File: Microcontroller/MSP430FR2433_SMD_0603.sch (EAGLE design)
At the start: 8 parts, among them IC2 MSP430FR2433IRGET, Q8 32.768

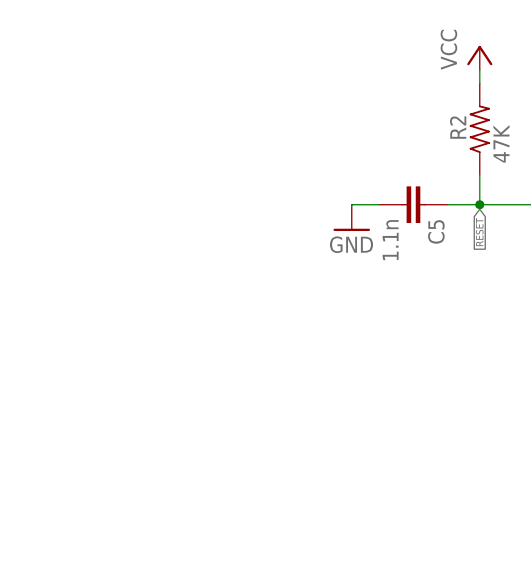
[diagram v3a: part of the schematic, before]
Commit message: masp430fr2433 modified
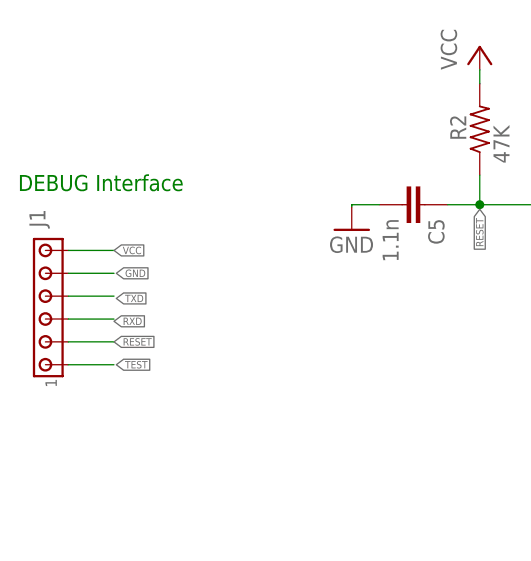
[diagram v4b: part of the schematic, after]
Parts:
- added J1: (no value), con-amp:MTA06-100
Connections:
- net GND: now also J1.5
- net RESET: now also J1.2
- net RXD: now also J1.3
- net TEST: now also J1.1
- net TXD: now also J1.4
- net VCC: now also J1.6
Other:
- note added: "DEBUG Interface"
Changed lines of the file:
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@@
 <part name="GND6" library="supply1" deviceset="GND" device=""/>
 <part name="GND7" library="supply1" deviceset="GND" device=""/>
+<part name="J1" library="con-amp" deviceset="MTA06-100" device=""/>
 </parts>
 <sheets>
 <sheet>
 <plain>
+<text x="78.232" y="136.144" size="1.778" layer="91">DEBUG Interface</text>
 </plain>
 <instances>
@@
 <instance part="GND6" gate="1" x="282.956" y="115.316"/>
 <instance part="GND7" gate="1" x="242.824" y="139.7" rot="R180"/>
+<instance part="J1" gate="G$1" x="81.28" y="121.92" rot="R90"/>
 </instances>
 <busses>
@@
 <pinref part="IC2" gate="G$1" pin="!RST!/NMI/SBWTDIO"/>
 <label x="129.54" y="134.112" size="0.8128" layer="95" rot="R270" xref="yes"/>
+</segment>
+<segment>
+<pinref part="J1" gate="G$1" pin="2"/>
+<wire x1="83.82" y1="119.38" x2="88.9" y2="119.38" width="0.1524" layer="91"/>
+<label x="88.9" y="119.38" size="0.8128" layer="95" xref="yes"/>
 </segment>
 </net>
@@
 <pinref part="GND7" gate="1" pin="GND"/>
 </segment>
+<segment>
+<pinref part="J1" gate="G$1" pin="5"/>
+<wire x1="83.82" y1="127" x2="88.9" y2="127" width="0.1524" layer="91"/>
+<label x="89.154" y="127" size="0.8128" layer="95" xref="yes"/>
+</segment>
 </net>
 <net name="VCC" class="0">
@@
 <pinref part="R2" gate="G$1" pin="2"/>
 <wire x1="129.54" y1="149.606" x2="129.54" y2="148.082" width="0.1524" layer="91"/>
+</segment>
+<segment>
+<pinref part="J1" gate="G$1" pin="6"/>
+<wire x1="83.82" y1="129.54" x2="88.9" y2="129.54" width="0.1524" layer="91"/>
+<label x="88.9" y="129.54" size="0.8128" layer="95" xref="yes"/>
 </segment>
 </net>
@@
 <label x="144.78" y="132.08" size="0.8128" layer="95" rot="R180" xref="yes"/>
 </segment>
+<segment>
+<pinref part="J1" gate="G$1" pin="1"/>
+<wire x1="83.82" y1="116.84" x2="88.9" y2="116.84" width="0.1524" layer="91"/>
+<label x="89.154" y="116.84" size="0.8128" layer="95" xref="yes"/>
+</segment>
 </net>
 <net name="TXD" class="0">
@@
 <wire x1="149.86" y1="129.54" x2="144.78" y2="129.54" width="0.1524" layer="91"/>
 <label x="144.78" y="129.54" size="0.8128" layer="95" rot="R180" xref="yes"/>
+</segment>
+<segment>
+<pinref part="J1" gate="G$1" pin="4"/>
+<wire x1="83.82" y1="124.46" x2="88.9" y2="124.46" width="0.1524" layer="91"/>
+<label x="89.154" y="124.206" size="0.8128" layer="95" xref="yes"/>
 </segment>
 </net>
@@
 <label x="144.78" y="127" size="0.8128" layer="95" rot="R180" xref="yes"/>
 </segment>
+<segment>
+<pinref part="J1" gate="G$1" pin="3"/>
+<wire x1="83.82" y1="121.92" x2="88.9" y2="121.92" width="0.1524" layer="91"/>
+<label x="88.9" y="121.666" size="0.8128" layer="95" xref="yes"/>
+</segment>
 </net>

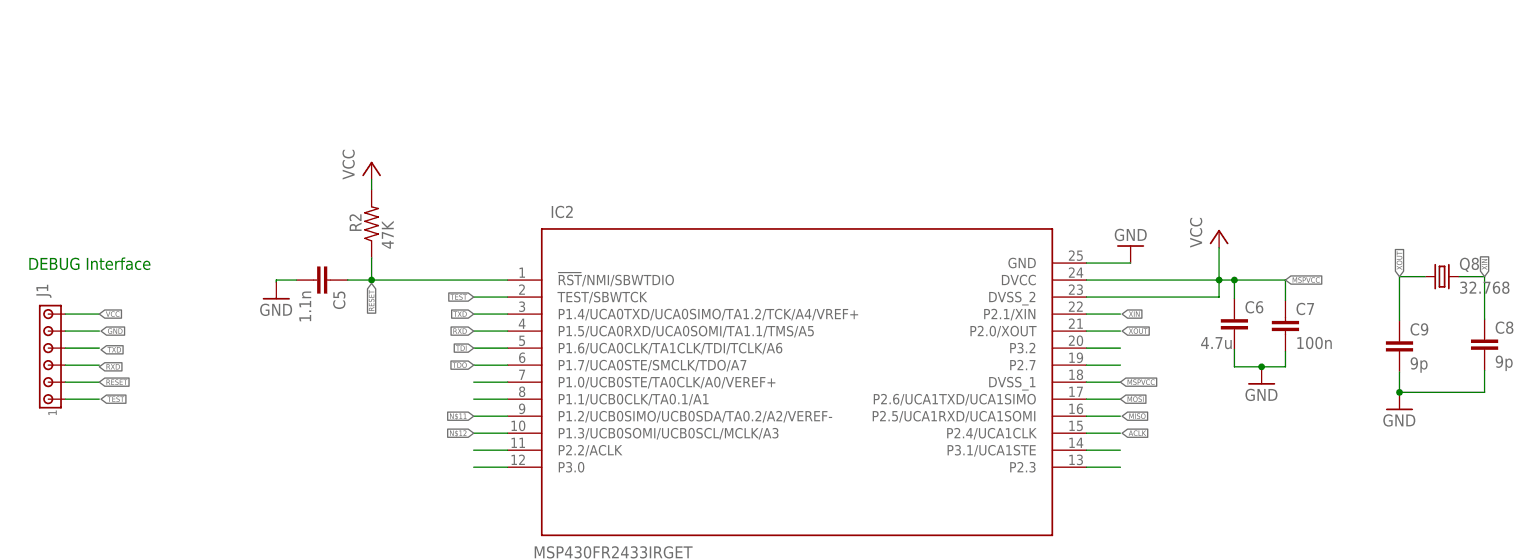
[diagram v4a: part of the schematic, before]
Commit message: masp430fr2433 modified
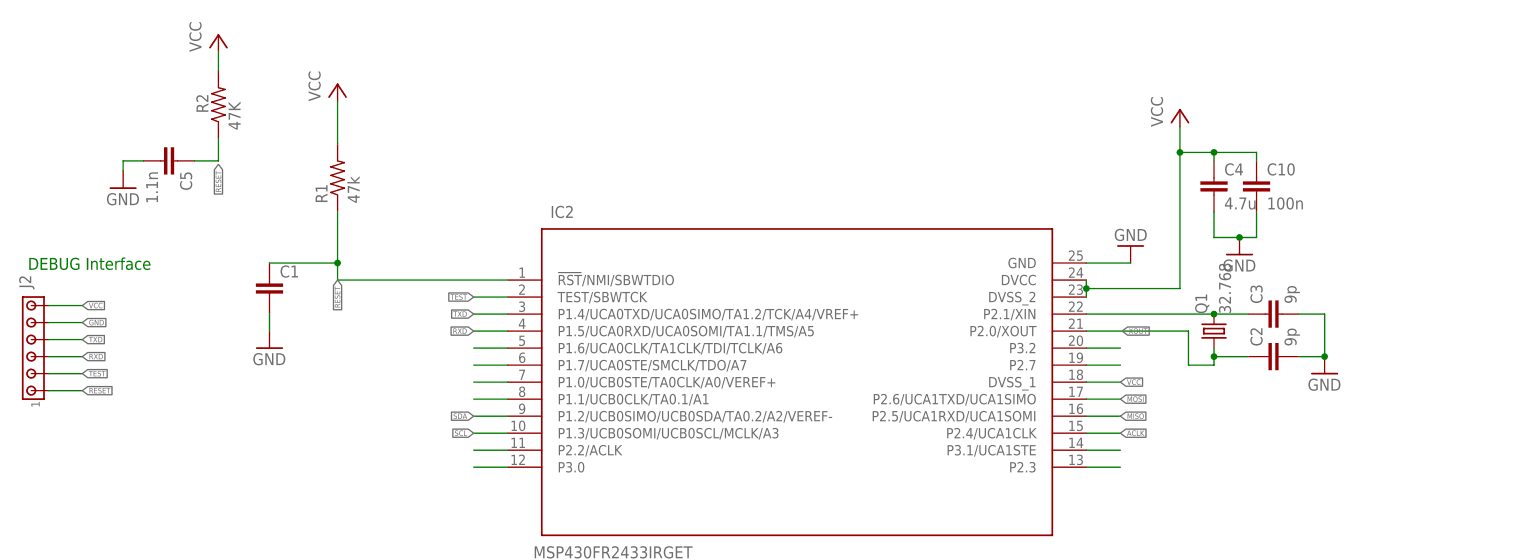
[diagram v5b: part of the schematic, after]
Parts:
- removed C6: 4.7u, rcl:C-EUC0402
- removed C7: 100n, rcl:C-EUC0402
- removed C8, C9: 9p, rcl:C-EUC0402
- removed J1: (no value), con-amp:MTA06-100
- removed Q8: 32.768, crystal:CRYTALTC26H
- added C1: (no value), rcl:C-EUC0402
- added C10: 100n, rcl:C-EUC0402
- added C2, C3: 9p, rcl:C-EUC0402
- added C4: 4.7u, rcl:C-EUC0402
- added J2: (no value), con-amp:MTA06-100
- added Q1: 32.768, crystal:CRYTALTC26H
- added R1: 47k, rcl:R-US_R0402
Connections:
- net N$11 renamed SDA
- net N$12 renamed SCL
- net TDI renamed N$7
- net TDO renamed N$8
- removed net MSPVCC: C6.1, C7.1, IC2.DVCC, IC2.DVSS_1, IC2.DVSS_2
- removed net XIN: C8.1, IC2.P2.1/XIN, Q8.2
- new net N$3: C3.1, IC2.P2.1/XIN, Q1.2
- net GND: now also C1.2, C10.2, C2.2, C3.2, C4.2, J2.5; no longer C6.2, C7.2, C8.2, C9.2, J1.5
- net RESET: now also C1.1, J2.1, R1.1; no longer J1.2
- net RXD: now also J2.3; no longer J1.3
- net TEST: now also J2.2; no longer J1.1
- net TXD: now also J2.4; no longer J1.4
- net VCC: now also C10.1, C4.1, IC2.DVCC, IC2.DVSS_1, IC2.DVSS_2, J2.6, R1.2; no longer J1.6
- net XOUT: now also C2.1, Q1.1; no longer C9.1, Q8.1
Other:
- moved on the sheet: C5, R2

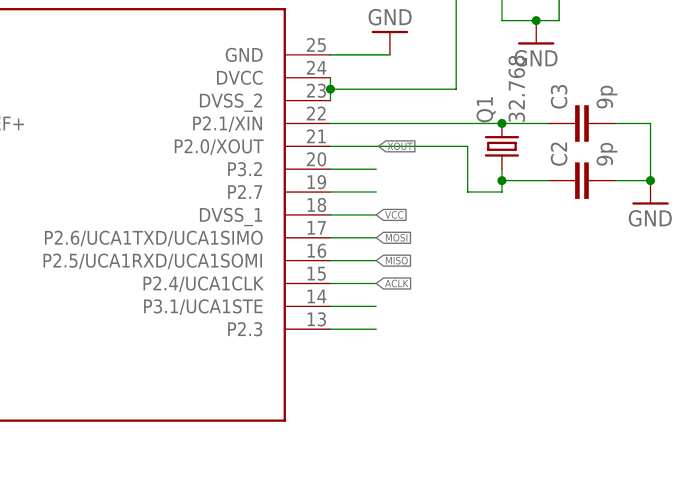
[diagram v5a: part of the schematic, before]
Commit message: masp430fr2433 modified
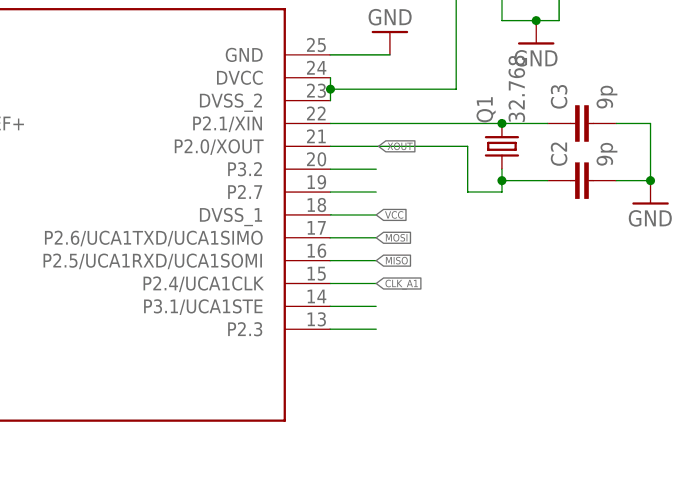
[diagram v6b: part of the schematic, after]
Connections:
- net ACLK renamed CLK_A1
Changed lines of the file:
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@@
 <setting verticaltext="up"/>
 </settings>
-<grid distance="0.05" unitdist="inch" unit="inch" style="lines" multiple="1" display="no" altdistance="0.01" altunitdist="inch" altunit="inch"/>
+<grid distance="0.1" unitdist="inch" unit="inch" style="lines" multiple="1" display="no" altdistance="0.01" altunitdist="inch" altunit="inch"/>
 <layers>
 <layer number="1" name="Top" color="4" fill="1" visible="no" active="no"/>
@@
 </segment>
 </net>
-<net name="ACLK" class="0">
+<net name="CLK_A1" class="0">
 <segment>
 <pinref part="IC2" gate="G$1" pin="P2.4/UCA1CLK"/>
